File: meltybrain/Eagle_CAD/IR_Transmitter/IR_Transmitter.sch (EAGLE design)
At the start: 0 parts

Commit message: Reverse polarity protection
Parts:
- added C1: 100p, rcl:C-USC0603
- added C41: 1u, rcl:C-USC0603
- added C44: 2.2u, rcl:C-USC0603
- added D1: SFH_4544, EmitterParts:SFH_4544
- added Q1: BSS806N, RoboJackets-Discrete:BSS806N
- added Q2: FQP47P06, EmitterParts:FQP47P06
- added R1: 6.8, rcl:R-US_R0603
- added R2: 500, rcl:R-US_R0603
- added U$1: ATTINY84, EmitterParts:ATTINY84
- added U1: LMH6612MAX/NOPB, Hocki_Library:LMH6612MAX/NOPB
- added U2: AP2210K-5.0TRG1, Hocki_Library:AP2210K-5.0TRG1
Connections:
- new net +5V: C44.1, D1.A, U$1.VCC, U1.V+, U2.OUT
- new net 9V: Q2.D
- new net GND: C1.2, C41.2, C44.2, Q2.G, R1.1, R2.1, U$1.GND, U1.INB+, U1.INB-, U1.V-, U2.GND
- new net N$1: Q1.S, R1.2, U1.INA-
- new net N$2: Q1.G, U1.OUTA
- new net N$3: R2.2, U1.OUTB
- new net N$4: U$1.PA5, U1.INA+
- new net N$5: D1.C, Q1.D
- new net N$6: C1.1, U2.BYP
- new net N$7: C41.1, Q2.S, U2.EN, U2.IN

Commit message: Connector progress
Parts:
- added CN1: (no value), Hocki_Library:JST_2PIN-SMT-RA
- added J1: 4PIN-0353620450, RoboJackets-Connectors:4PIN-0353620450
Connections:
- new net N$8: U$1.PA6
- new net N$9: U$1.PB3
- net 9V: now also CN1.2, CN1.SHIELD
- net GND: now also CN1.1
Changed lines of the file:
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@@
 <part name="GND4" library="SparkFun-PowerSymbols" library_urn="urn:adsk.eagle:library:530" deviceset="GND" device=""/>
 <part name="Q2" library="EmitterParts" deviceset="FQP47P06" device=""/>
+<part name="CN1" library="Hocki_Library" deviceset="JST_2PIN" device="-SMT-RA"/>
+<part name="J1" library="RoboJackets-Connectors" deviceset="4PIN-03536?" device="20450"/>
 </parts>
 <sheets>
@@
 <attribute name="VALUE" x="-34.29" y="41.91" size="1.778" layer="96" rot="MR90" align="top-left"/>
 <attribute name="NAME" x="-26.67" y="41.91" size="1.778" layer="95" rot="MR90"/>
+</instance>
+<instance part="CN1" gate="G$1" x="-50.8" y="48.26" smashed="yes" rot="R180">
+<attribute name="NAME" x="-44.45" y="42.545" size="1.778" layer="95" rot="R180"/>
+<attribute name="VALUE" x="-44.45" y="55.88" size="1.778" layer="96" rot="R180"/>
+</instance>
+<instance part="J1" gate="G$1" x="-78.74" y="20.32" smashed="yes">
+<attribute name="NAME" x="-85.09" y="28.575" size="1.778" layer="95"/>
+<attribute name="VALUE" x="-85.09" y="12.7" size="1.778" layer="96"/>
 </instance>
 </instances>
@@
 <pinref part="Q2" gate="G$1" pin="G"/>
 <wire x1="-27.94" y1="43.18" x2="-27.94" y2="48.26" width="0.1524" layer="91"/>
+<pinref part="CN1" gate="G$1" pin="1"/>
+<wire x1="-48.26" y1="45.72" x2="-35.56" y2="45.72" width="0.1524" layer="91"/>
+<wire x1="-35.56" y1="45.72" x2="-35.56" y2="43.18" width="0.1524" layer="91"/>
+<wire x1="-35.56" y1="43.18" x2="-27.94" y2="43.18" width="0.1524" layer="91"/>
+<junction x="-27.94" y="43.18"/>
 </segment>
 <segment>
@@
 <pinref part="Q2" gate="G$1" pin="D"/>
 <wire x1="-35.56" y1="63.5" x2="-35.56" y2="53.34" width="0.1524" layer="91"/>
-</segment>
-</net>
+<pinref part="CN1" gate="G$1" pin="2"/>
+<wire x1="-48.26" y1="48.26" x2="-35.56" y2="48.26" width="0.1524" layer="91"/>
+<wire x1="-35.56" y1="48.26" x2="-35.56" y2="50.8" width="0.1524" layer="91"/>
+<junction x="-35.56" y="53.34"/>
+<pinref part="CN1" gate="G$1" pin="SHIELD"/>
+<wire x1="-35.56" y1="50.8" x2="-35.56" y2="53.34" width="0.1524" layer="91"/>
+<wire x1="-48.26" y1="50.8" x2="-35.56" y2="50.8" width="0.1524" layer="91"/>
+<junction x="-35.56" y="50.8"/>
+</segment>
+</net>
+<net name="N$8" class="0">
+<segment>
+<pinref part="U$1" gate="G$1" pin="PA6"/>
+<wire x1="-53.34" y1="2.54" x2="-58.42" y2="2.54" width="0.1524" layer="91"/>
+</segment>
+</net>
+<net name="N$9" class="0">
+<segment>
+<pinref part="U$1" gate="G$1" pin="PB3"/>
+<wire x1="-53.34" y1="17.78" x2="-58.42" y2="17.78" width="0.1524" layer="91"/>
+</segment>
+</net>

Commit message: Connector progress
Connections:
- removed net N$4: U$1.PA5, U1.INA+
- removed net N$8: U$1.PA6
- removed net N$9: U$1.PB3
- new net MISO: J1.2, U$1.PA5, U1.INA+
- new net MOSI: J1.1, U$1.PA6
- new net SCK: J1.3, U$1.PA4
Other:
- moved on the sheet: D1, J1, Q1, R1, R2, U1

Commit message: Schematic Finished, Board Routed
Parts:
- added C2: 0.1u, rcl:C-USC0603
- J1: value 4PIN-0353620450 -> AVR_SPI_PROG_3X2NS; device RoboJackets-Connectors:4PIN-0353620450 -> SparkFun-Connectors:AVR_SPI_PROG_3X2NS
- Q2: value FQP47P06 -> FDN352AP; device EmitterParts:FQP47P06 -> EmitterParts:FDN352AP
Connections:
- new net OUT: U$1.PB2, U1.INA+
- new net RST: J1.5, U$1.PB3
- net +5V: now also C2.1, J1.2
- net 9V: no longer CN1.SHIELD
- net GND: now also C2.2, J1.6
- net MISO: now also J1.1; no longer J1.2, U1.INA+
- net MOSI: now also J1.4; no longer J1.1
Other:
- moved on the sheet: U$1
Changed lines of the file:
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@@
 <part name="C44" library="rcl" library_urn="urn:adsk.eagle:library:334" deviceset="C-US" device="C0603" package3d_urn="urn:adsk.eagle:package:23616/2" value="2.2u"/>
 <part name="GND4" library="SparkFun-PowerSymbols" library_urn="urn:adsk.eagle:library:530" deviceset="GND" device=""/>
-<part name="Q2" library="EmitterParts" deviceset="FQP47P06" device=""/>
+<part name="Q2" library="EmitterParts" deviceset="FDN352AP" device=""/>
 <part name="CN1" library="Hocki_Library" deviceset="JST_2PIN" device="-SMT-RA"/>
-<part name="J1" library="RoboJackets-Connectors" deviceset="4PIN-03536?" device="20450"/>
+<part name="J1" library="SparkFun-Connectors" library_urn="urn:adsk.eagle:library:513" deviceset="AVR_SPI_PROG_3X2" device="NS" package3d_urn="urn:adsk.eagle:package:38013/1"/>
+<part name="P+4" library="supply1" library_urn="urn:adsk.eagle:library:371" deviceset="+5V" device=""/>
+<part name="GND5" library="SparkFun-PowerSymbols" library_urn="urn:adsk.eagle:library:530" deviceset="GND" device=""/>
+<part name="C2" library="rcl" library_urn="urn:adsk.eagle:library:334" deviceset="C-US" device="C0603" package3d_urn="urn:adsk.eagle:package:23616/2" value="0.1u"/>
 </parts>
 <sheets>
@@
 <attribute name="VALUE" x="50.8" y="25.4" size="1.778" layer="96" rot="R90"/>
 </instance>
-<instance part="U$1" gate="G$1" x="-40.64" y="17.78" smashed="yes">
-<attribute name="NAME" x="-48.26" y="35.56" size="2.54" layer="95"/>
-<attribute name="VALUE" x="-48.26" y="0" size="2.54" layer="96" align="top-left"/>
-</instance>
-<instance part="P+2" gate="1" x="-58.42" y="45.72" smashed="yes">
-<attribute name="VALUE" x="-60.96" y="40.64" size="1.778" layer="96" rot="R90"/>
-</instance>
-<instance part="GND2" gate="1" x="-22.86" y="30.48" smashed="yes">
-<attribute name="VALUE" x="-22.86" y="30.226" size="1.778" layer="96" align="top-center"/>
+<instance part="U$1" gate="G$1" x="-43.18" y="0" smashed="yes">
+<attribute name="NAME" x="-50.8" y="17.78" size="2.54" layer="95"/>
+<attribute name="VALUE" x="-50.8" y="-17.78" size="2.54" layer="96" align="top-left"/>
+</instance>
+<instance part="P+2" gate="1" x="-60.96" y="27.94" smashed="yes">
+<attribute name="VALUE" x="-63.5" y="22.86" size="1.778" layer="96" rot="R90"/>
+</instance>
+<instance part="GND2" gate="1" x="-25.4" y="12.7" smashed="yes">
+<attribute name="VALUE" x="-25.4" y="12.446" size="1.778" layer="96" align="top-center"/>
 </instance>
 <instance part="U2" gate="G$1" x="-2.54" y="50.8" smashed="yes">
@@
 <attribute name="VALUE" x="-44.45" y="55.88" size="1.778" layer="96" rot="R180"/>
 </instance>
-<instance part="J1" gate="G$1" x="-81.28" y="15.24" smashed="yes">
-<attribute name="NAME" x="-87.63" y="23.495" size="1.778" layer="95"/>
-<attribute name="VALUE" x="-87.63" y="7.62" size="1.778" layer="96"/>
+<instance part="J1" gate="G$1" x="-106.68" y="7.62" smashed="yes">
+<attribute name="NAME" x="-111.76" y="13.208" size="1.778" layer="95" font="vector"/>
+<attribute name="VALUE" x="-111.76" y="0.254" size="1.778" layer="96" font="vector"/>
+</instance>
+<instance part="P+4" gate="1" x="-91.44" y="22.86" smashed="yes">
+<attribute name="VALUE" x="-93.98" y="17.78" size="1.778" layer="96" rot="R90"/>
+</instance>
+<instance part="GND5" gate="1" x="-91.44" y="2.54" smashed="yes">
+<attribute name="VALUE" x="-91.44" y="2.286" size="1.778" layer="96" align="top-center"/>
+</instance>
+<instance part="C2" gate="G$1" x="-43.18" y="25.4" smashed="yes" rot="R90">
+<attribute name="NAME" x="-45.085" y="25.146" size="1.778" layer="95" rot="R270"/>
+<attribute name="VALUE" x="-41.021" y="25.146" size="1.778" layer="96" rot="R270"/>
 </instance>
 </instances>
@@
 <segment>
 <pinref part="U$1" gate="G$1" pin="GND"/>
-<wire x1="-27.94" y1="33.02" x2="-22.86" y2="33.02" width="0.1524" layer="91"/>
+<wire x1="-30.48" y1="15.24" x2="-25.4" y2="15.24" width="0.1524" layer="91"/>
 <pinref part="GND2" gate="1" pin="GND"/>
+<pinref part="C2" gate="G$1" pin="2"/>
+<wire x1="-38.1" y1="25.4" x2="-25.4" y2="25.4" width="0.1524" layer="91"/>
+<wire x1="-25.4" y1="25.4" x2="-25.4" y2="15.24" width="0.1524" layer="91"/>
+<junction x="-25.4" y="15.24"/>
 </segment>
 <segment>
@@
 <junction x="17.78" y="43.18"/>
 </segment>
+<segment>
+<pinref part="J1" gate="G$1" pin="6"/>
+<wire x1="-96.52" y1="5.08" x2="-91.44" y2="5.08" width="0.1524" layer="91"/>
+<pinref part="GND5" gate="1" pin="GND"/>
+</segment>
 </net>
 <net name="N$3" class="0">
@@
 <segment>
 <pinref part="U$1" gate="G$1" pin="VCC"/>
-<wire x1="-53.34" y1="33.02" x2="-58.42" y2="33.02" width="0.1524" layer="91"/>
+<wire x1="-55.88" y1="15.24" x2="-60.96" y2="15.24" width="0.1524" layer="91"/>
 <pinref part="P+2" gate="1" pin="+5V"/>
-<wire x1="-58.42" y1="33.02" x2="-58.42" y2="43.18" width="0.1524" layer="91"/>
+<wire x1="-60.96" y1="15.24" x2="-60.96" y2="25.4" width="0.1524" layer="91"/>
+<pinref part="C2" gate="G$1" pin="1"/>
+<wire x1="-45.72" y1="25.4" x2="-60.96" y2="25.4" width="0.1524" layer="91"/>
+<junction x="-60.96" y="25.4"/>
 </segment>
 <segment>
@@
 <pinref part="C44" gate="G$1" pin="1"/>
 <junction x="17.78" y="53.34"/>
+</segment>
+<segment>
+<pinref part="J1" gate="G$1" pin="2"/>
+<wire x1="-96.52" y1="10.16" x2="-91.44" y2="10.16" width="0.1524" layer="91"/>
+<pinref part="P+4" gate="1" pin="+5V"/>
+<wire x1="-91.44" y1="20.32" x2="-91.44" y2="10.16" width="0.1524" layer="91"/>
 </segment>
 </net>
@@
 <pinref part="CN1" gate="G$1" pin="2"/>
 <wire x1="-48.26" y1="48.26" x2="-35.56" y2="48.26" width="0.1524" layer="91"/>
-<wire x1="-35.56" y1="48.26" x2="-35.56" y2="50.8" width="0.1524" layer="91"/>
 <junction x="-35.56" y="53.34"/>
-<pinref part="CN1" gate="G$1" pin="SHIELD"/>
-<wire x1="-35.56" y1="50.8" x2="-35.56" y2="53.34" width="0.1524" layer="91"/>
-<wire x1="-48.26" y1="50.8" x2="-35.56" y2="50.8" width="0.1524" layer="91"/>
-<junction x="-35.56" y="50.8"/>
+<wire x1="-35.56" y1="48.26" x2="-35.56" y2="53.34" width="0.1524" layer="91"/>
 </segment>
 </net>
@@
 <segment>
 <pinref part="U$1" gate="G$1" pin="PA6"/>
-<wire x1="-53.34" y1="2.54" x2="-58.42" y2="2.54" width="0.1524" layer="91"/>
-<label x="-58.42" y="2.54" size="1.778" layer="95" rot="R180" xref="yes"/>
-</segment>
+<wire x1="-55.88" y1="-15.24" x2="-60.96" y2="-15.24" width="0.1524" layer="91"/>
+<label x="-60.96" y="-15.24" size="1.778" layer="95" rot="R180" xref="yes"/>
+</segment>
+<segment>
+<pinref part="J1" gate="G$1" pin="4"/>
+<wire x1="-96.52" y1="7.62" x2="-91.44" y2="7.62" width="0.1524" layer="91"/>
+<label x="-91.44" y="7.62" size="1.778" layer="95" xref="yes"/>
+</segment>
+</net>
+<net name="SCK" class="0">
+<segment>
+<pinref part="U$1" gate="G$1" pin="PA4"/>
+<wire x1="-30.48" y1="-10.16" x2="-25.4" y2="-10.16" width="0.1524" layer="91"/>
+<label x="-25.4" y="-10.16" size="1.778" layer="95" xref="yes"/>
+</segment>
+<segment>
+<pinref part="J1" gate="G$1" pin="3"/>
+<wire x1="-114.3" y1="7.62" x2="-119.38" y2="7.62" width="0.1524" layer="91"/>
+<label x="-119.38" y="7.62" size="1.778" layer="95" rot="R180" xref="yes"/>
+</segment>
+</net>
+<net name="MISO" class="0">
 <segment>
 <pinref part="J1" gate="G$1" pin="1"/>
-<wire x1="-83.82" y1="20.32" x2="-91.44" y2="20.32" width="0.1524" layer="91"/>
-<label x="-91.44" y="20.32" size="1.778" layer="95" rot="R180" xref="yes"/>
-</segment>
-</net>
-<net name="SCK" class="0">
-<segment>
-<pinref part="U$1" gate="G$1" pin="PA4"/>
-<wire x1="-27.94" y1="7.62" x2="-22.86" y2="7.62" width="0.1524" layer="91"/>
-<label x="-22.86" y="7.62" size="1.778" layer="95" xref="yes"/>
-</segment>
-<segment>
-<pinref part="J1" gate="G$1" pin="3"/>
-<wire x1="-83.82" y1="15.24" x2="-91.44" y2="15.24" width="0.1524" layer="91"/>
-<label x="-91.44" y="15.24" size="1.778" layer="95" rot="R180" xref="yes"/>
-</segment>
-</net>
-<net name="MISO" class="0">
+<wire x1="-114.3" y1="10.16" x2="-119.38" y2="10.16" width="0.1524" layer="91"/>
+<label x="-119.38" y="10.16" size="1.778" layer="95" rot="R180" xref="yes"/>
+</segment>
 <segment>
 <pinref part="U$1" gate="G$1" pin="PA5"/>
-<wire x1="-27.94" y1="2.54" x2="-22.86" y2="2.54" width="0.1524" layer="91"/>
-<label x="-22.86" y="2.54" size="1.778" layer="95" xref="yes"/>
+<wire x1="-30.48" y1="-15.24" x2="-25.4" y2="-15.24" width="0.1524" layer="91"/>
+<label x="-25.4" y="-15.24" size="1.778" layer="95" xref="yes"/>
+</segment>
+</net>
+<net name="RST" class="0">
+<segment>
+<pinref part="U$1" gate="G$1" pin="PB3"/>
+<wire x1="-55.88" y1="0" x2="-60.96" y2="0" width="0.1524" layer="91"/>
+<label x="-60.96" y="0" size="1.778" layer="95" rot="R180" xref="yes"/>
+</segment>
+<segment>
+<pinref part="J1" gate="G$1" pin="5"/>
+<wire x1="-114.3" y1="5.08" x2="-119.38" y2="5.08" width="0.1524" layer="91"/>
+<label x="-119.38" y="5.08" size="1.778" layer="95" rot="R180" xref="yes"/>
+</segment>
+</net>
+<net name="OUT" class="0">
+<segment>
+<pinref part="U$1" gate="G$1" pin="PB2"/>
+<wire x1="-55.88" y1="-5.08" x2="-60.96" y2="-5.08" width="0.1524" layer="91"/>
+<label x="-60.96" y="-5.08" size="1.778" layer="95" rot="R180" xref="yes"/>
 </segment>
 <segment>
@@
 <label x="10.16" y="2.54" size="1.778" layer="95" rot="R180" xref="yes"/>
 </segment>
-<segment>
-<pinref part="J1" gate="G$1" pin="2"/>
-<wire x1="-83.82" y1="17.78" x2="-91.44" y2="17.78" width="0.1524" layer="91"/>
-<label x="-91.44" y="17.78" size="1.778" layer="95" rot="R180" xref="yes"/>
-</segment>
-</net>
+</net>

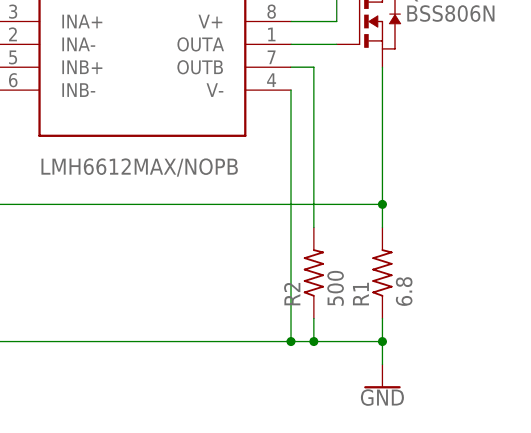
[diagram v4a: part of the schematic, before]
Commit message: Replaced resistor R1 with 1.5 ohm 0402 Resistor
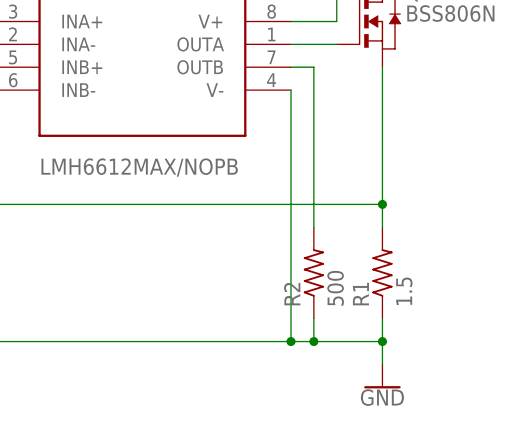
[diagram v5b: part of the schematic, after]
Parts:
- R1: value 6.8 -> 1.5; device rcl:R-US_R0603 -> rcl:R-US_R0402
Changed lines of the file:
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@@
 <layers>
 <layer number="1" name="Top" color="4" fill="1" visible="no" active="no"/>
+<layer number="2" name="Route2" color="1" fill="3" visible="no" active="no"/>
+<layer number="3" name="Route3" color="4" fill="3" visible="no" active="no"/>
+<layer number="4" name="Route4" color="1" fill="4" visible="no" active="no"/>
+<layer number="5" name="Route5" color="4" fill="4" visible="no" active="no"/>
+<layer number="6" name="Route6" color="1" fill="8" visible="no" active="no"/>
+<layer number="7" name="Route7" color="4" fill="8" visible="no" active="no"/>
+<layer number="8" name="Route8" color="1" fill="2" visible="no" active="no"/>
+<layer number="9" name="Route9" color="4" fill="2" visible="no" active="no"/>
+<layer number="10" name="Route10" color="1" fill="7" visible="no" active="no"/>
+<layer number="11" name="Route11" color="4" fill="7" visible="no" active="no"/>
+<layer number="12" name="Route12" color="1" fill="5" visible="no" active="no"/>
+<layer number="13" name="Route13" color="4" fill="5" visible="no" active="no"/>
+<layer number="14" name="Route14" color="1" fill="6" visible="no" active="no"/>
+<layer number="15" name="Route15" color="4" fill="6" visible="no" active="no"/>
 <layer number="16" name="Bottom" color="1" fill="1" visible="no" active="no"/>
 <layer number="17" name="Pads" color="2" fill="1" visible="no" active="no"/>
@@
 <part name="Q1" library="RoboJackets-Discrete" deviceset="BSS806N" device=""/>
 <part name="U1" library="Hocki_Library" deviceset="LMH6612MAX/NOPB" device=""/>
-<part name="R1" library="rcl" library_urn="urn:adsk.eagle:library:334" deviceset="R-US_" device="R0603" package3d_urn="urn:adsk.eagle:package:23555/3" value="6.8"/>
+<part name="R1" library="rcl" library_urn="urn:adsk.eagle:library:334" deviceset="R-US_" device="R0402" package3d_urn="urn:adsk.eagle:package:23547/3" value="1.5"/>
 <part name="GND1" library="SparkFun-PowerSymbols" library_urn="urn:adsk.eagle:library:530" deviceset="GND" device=""/>
 <part name="R2" library="rcl" library_urn="urn:adsk.eagle:library:334" deviceset="R-US_" device="R0603" package3d_urn="urn:adsk.eagle:package:23555/3" value="500"/>
